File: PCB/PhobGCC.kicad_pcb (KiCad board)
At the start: 2 copper layers, 125.5 x 72.9 mm, 43 parts, among them J1 Conn_01x06_Female, J2 Conn_01x04_Female, J3 Conn_01x01_Male, J4 Conn_01x01_Male, J6 10118194-0001LF, SW1 A, SW10 Dup, SW11 Dright, SW12 Ddown, SW2 B, SW3 X, SW4 Y, SW5 Start, SW6 L, SW7 R, SW8 1825027-5, SW9 Dleft, U1 Teensy3.2, U2 Stickbox_Assembly

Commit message: Trying again to get ready for removing unneeded kicad files
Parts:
- added G***: LOGO, Gamecube MB:Ghost Logo, F.Cu at (55.0, 73.5)
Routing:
- net /Stick_y: track 48.7 -> 48.2 mm
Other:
- net class Default: clearance 0.1525 -> 0.25
- net class USB added: clearance 0.15, trace_width 0.25, via_dia 0.8, via_drill 0.4
- rule trace_clearance: 0.1525 -> 0.25
- board text added: "20211226"
- board text added: "PhobGCC 1.0"

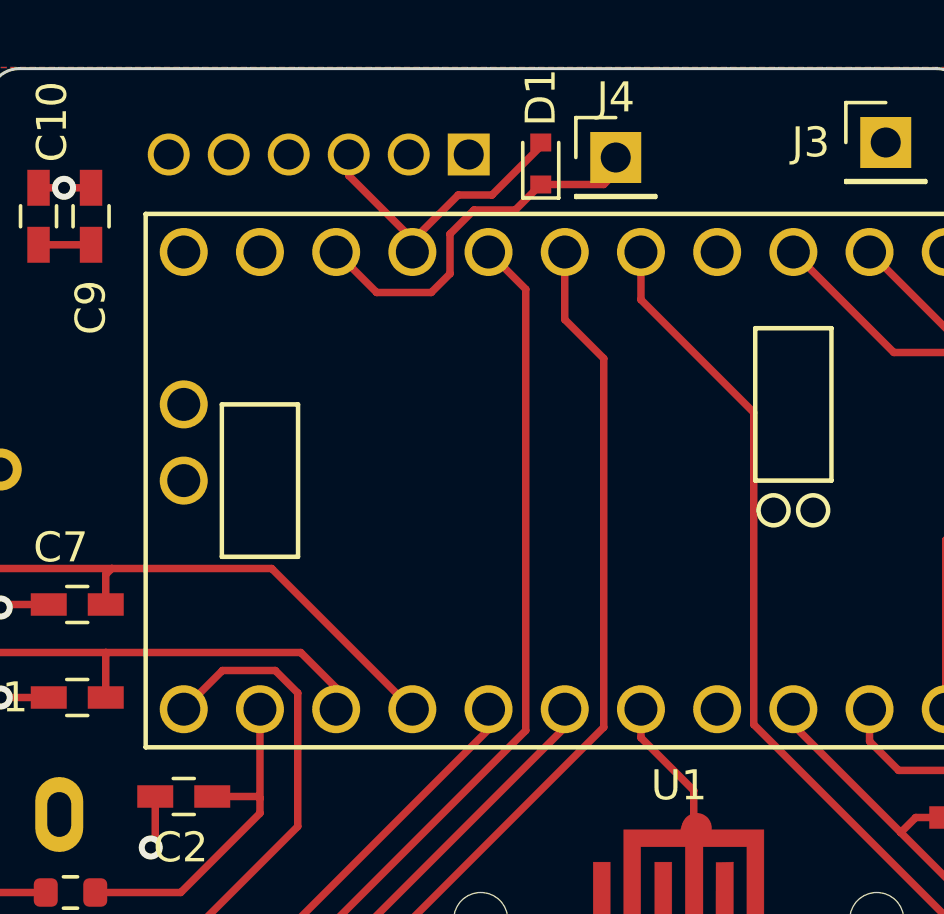
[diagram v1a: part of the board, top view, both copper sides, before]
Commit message: Changed schematic so that it "should" work with a teensy 3.2 or 4.0. Will require the pins of 2 of the d-pad buttons to be updated in the software.
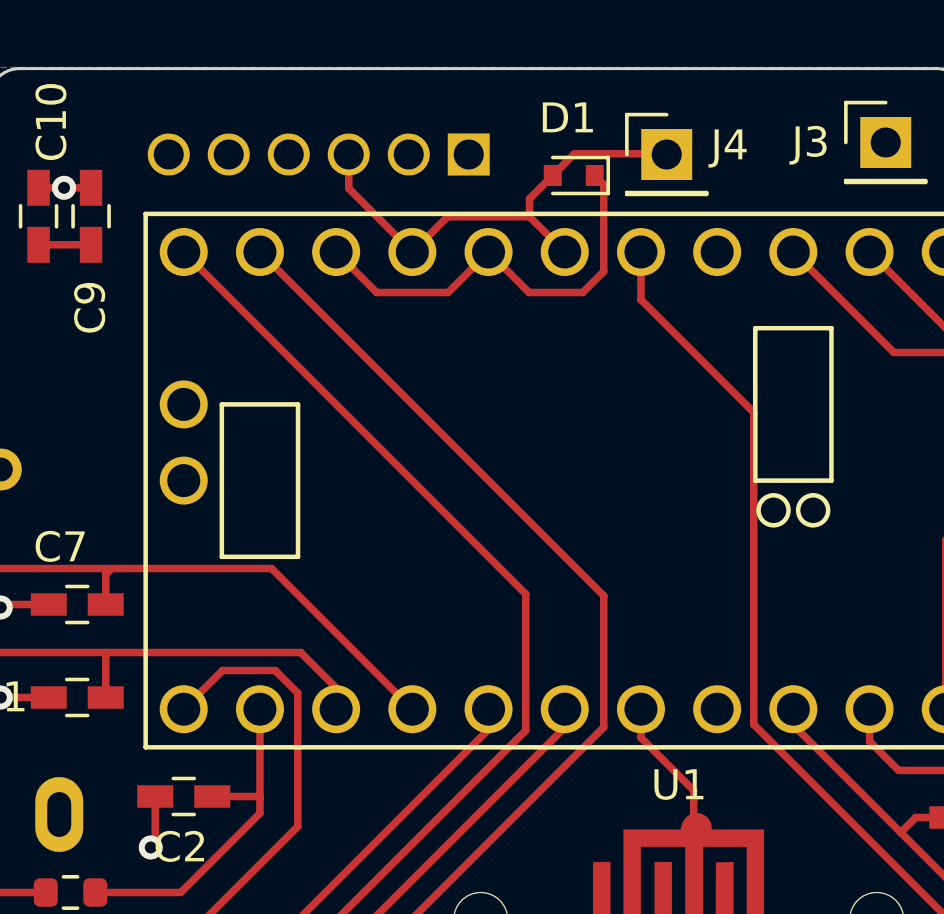
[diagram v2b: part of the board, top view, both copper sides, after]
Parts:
- moved J4 1.70 mm to (112.2, 52.9)
- moved D1 1.17 mm to (109.1, 53.6), turned to 180 degrees
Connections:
- J1 pad 2: (no net) -> +5V
- J4 pad 1: /TX -> /RX
- J6 pad 1: (no net) -> Net-(J6-Pad1)
- J6 pad 4: (no net) -> Net-(J6-Pad4)
- U1 pad 10: /Ddown -> /TX
- U1 pad 13: (no net) -> /Dright
- U1 pad 14: (no net) -> /Ddown
- U1 pad 27: (no net) -> Net-(U1-Pad27)
- U1 pad 32: (no net) -> Net-(U1-Pad32)
- U1 pad 33: (no net) -> Net-(U1-Pad33)
- U1 pad 7: (no net) -> Net-(U1-Pad7)
- U1 pad 9: /Dright -> /RX
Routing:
- net /RX: track 10.2 -> 15.8 mm
- net /Ddown: track 70.9 -> 75.1 mm
- net /Dright: track 63.4 -> 67.6 mm
- net /TX: track 12.4 -> 14.2 mm
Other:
- rule trace_min: 0.2 -> 0
